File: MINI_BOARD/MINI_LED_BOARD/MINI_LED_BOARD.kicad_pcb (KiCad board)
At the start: 2 copper layers, 75 x 15 mm, 47 parts, among them J1 Conn_ARM_SWD_TagConnect_TC203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, J2 430450428, J3 Conn_01x03_Socket, U1 MSPM0C1103SDDFR, U2 TCAN334, U4 TPS76333DBVR

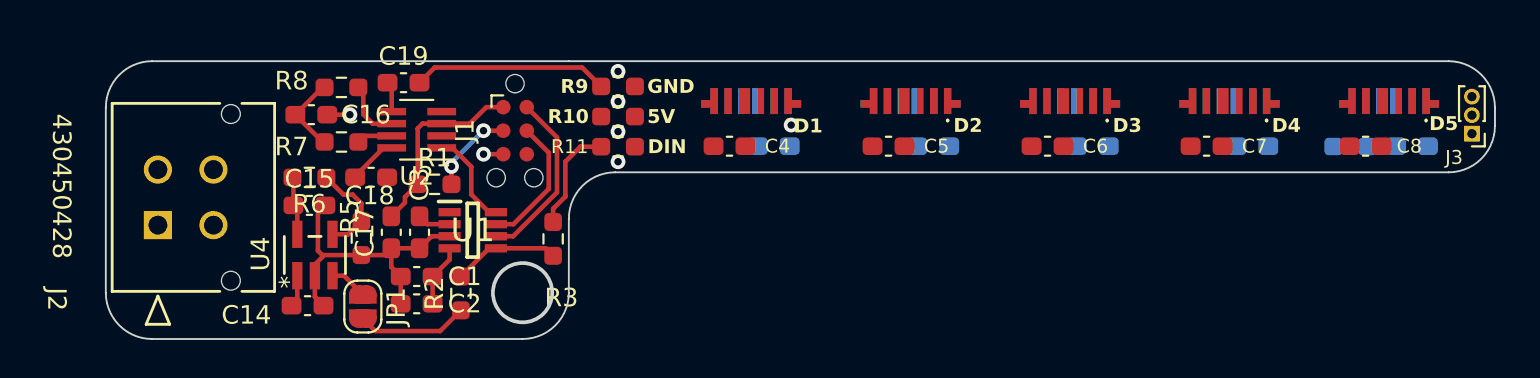
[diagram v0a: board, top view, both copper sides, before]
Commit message: Complete MCU side routing
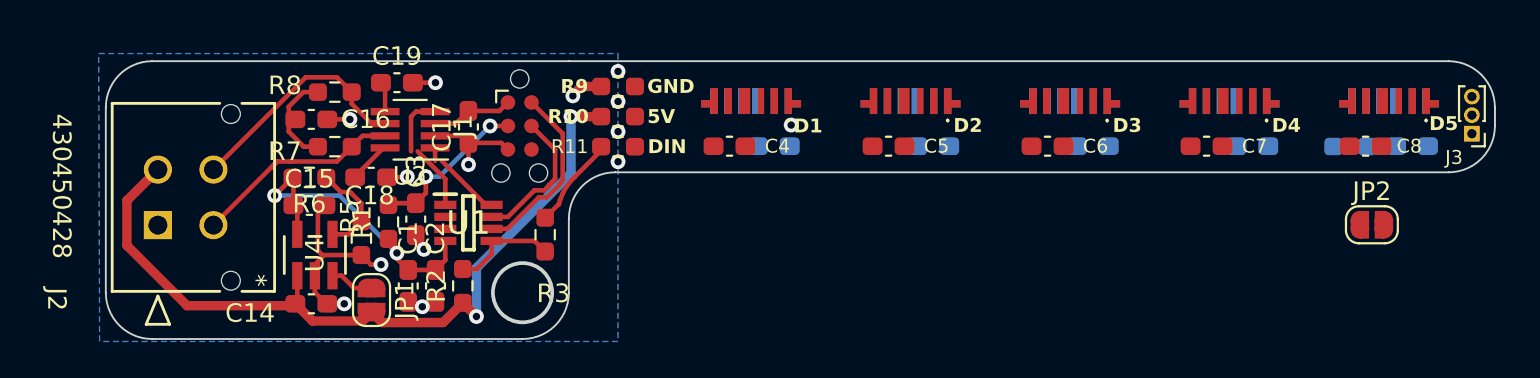
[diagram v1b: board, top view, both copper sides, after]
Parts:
- added JP2: SolderJumper_2_Open, Jumper:SolderJumper-2_P1.3mm_Open_RoundedPad1.0x1.5mm, F.Cu at (116.1, 61.9)
- moved C17 7.05 mm to (67.4, 56.6)
- moved R1 3.21 mm to (63.0, 61.8), turned to 90 degrees
- moved C2 1.40 mm to (65.6, 65.2), turned to -90 degrees
- moved C3 0.74 mm to (64.5, 61.6)
- moved C1 0.68 mm to (64.1, 65.2), turned to -90 degrees
- moved JP1 0.59 mm to (62.1, 66.0)
- moved R3 0.49 mm to (71.5, 62.5)
- moved U1 0.46 mm to (67.4, 61.8)
- moved R7 0.44 mm to (60.1, 57.7)
- moved R8 0.44 mm to (60.1, 54.8)
- moved R2 0.42 mm to (67.1, 65.2)
- moved J1 0.36 mm to (70.1, 56.6)
- moved C19 0.36 mm to (63.5, 54.3)
- moved U2 0.36 mm to (64.2, 56.8)
- moved C16 0.25 mm to (58.9, 56.2)
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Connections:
- J2 pad 3: Net-(U2-CANL) -> Net-(U2-CANH)
- J2 pad 4: Net-(U2-CANH) -> Net-(U2-CANL)
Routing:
- net +5V: track 7.79 -> 42.7 mm, vias 0 -> 2
- net Net-(U2-CANH): track 1.94 -> 11.7 mm
- net Net-(U2-CANL): track 3.36 -> 12.7 mm
- net Net-(U1-PA27_/_A0/UART_TX): track 0.00 -> 6.79 mm
- net GND: track 29.6 -> 23.9 mm, vias 2 -> 9
- net +3.3V: track 17.0 -> 22.2 mm, vias 0 -> 2
- net Net-(J1-~{RESET}): track 6.48 -> 9.10 mm
- net Net-(U1-PA24_/_A3/UART_RX): track 5.24 -> 4.38 mm
- net Net-(R11-Pad2): track 5.80 -> 5.00 mm
- net Net-(C16-Pad1): track 4.37 -> 5.16 mm
- net Net-(J1-SWCLK): track 7.27 -> 7.95 mm
- added copper zone on B.Cu, net GND

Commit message: Route LED side
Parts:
- removed JP2: SolderJumper_2_Open, Jumper:SolderJumper-2_P1.3mm_Open_RoundedPad1.0x1.5mm
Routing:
- net VDD: track 0.00 -> 129.1 mm, vias 0 -> 2
- net Net-(D10-DIN): track 0.00 -> 21.1 mm
- net Net-(D7-DOUT): track 0.00 -> 20.6 mm
- net GND2: track 0.00 -> 18.4 mm, vias 0 -> 1
- net Net-(D2-DOUT): track 0.00 -> 7.50 mm
- net Net-(D1-DOUT): track 0.00 -> 7.48 mm
- net Net-(D3-DOUT): track 0.00 -> 7.47 mm
- net Net-(D4-DOUT): track 0.00 -> 7.45 mm
- net Net-(D1-DIN): track 0.00 -> 4.79 mm
- net Net-(D10-DOUT): track 0.00 -> 4.20 mm
- net (no net): vias 5 -> 4
- added copper zone on B.Cu, net GND2
- added copper zone on F.Cu, net GND2

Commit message: Fix mcu side routing and update mcu-led jumper resistor pads
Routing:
- net +3.3V: track 22.2 -> 33.6 mm, vias 2 -> 3
- net GND: track 23.9 -> 24.9 mm, vias 9 -> 10
- net GND2: track 18.4 -> 19.1 mm

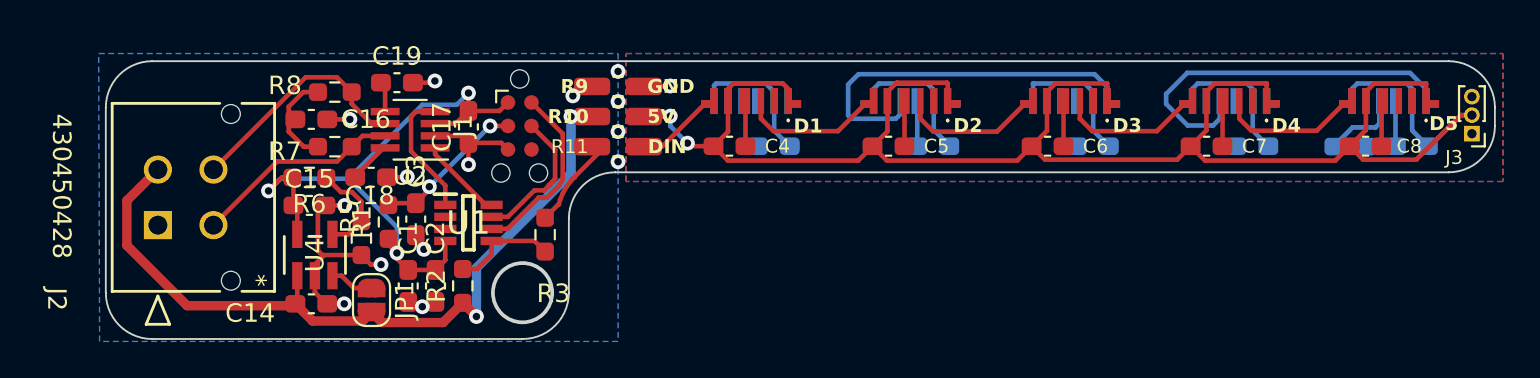
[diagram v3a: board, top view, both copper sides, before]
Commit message: More LED side routing changes
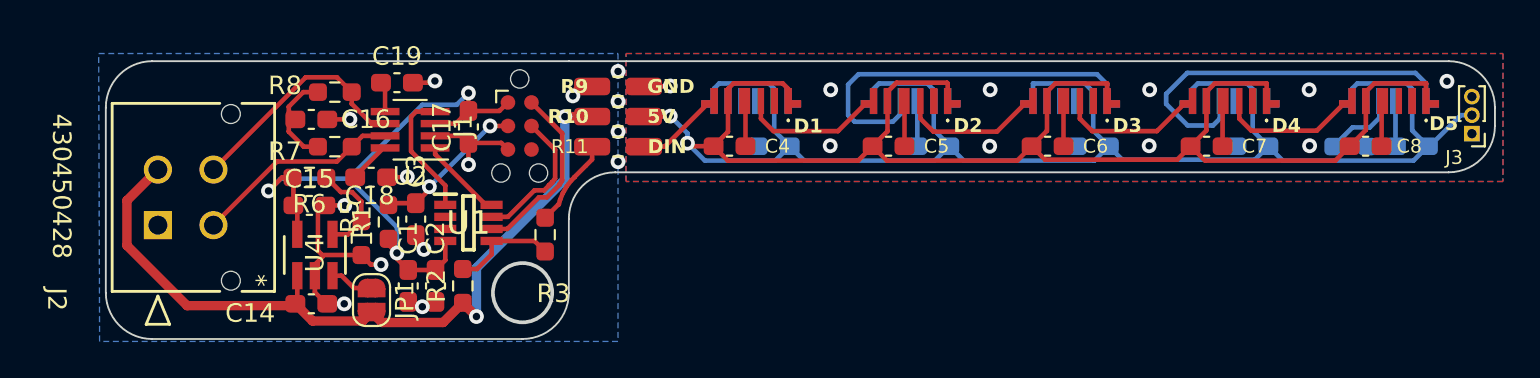
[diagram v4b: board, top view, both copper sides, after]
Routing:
- net VDD: track 129.4 -> 164.7 mm
- net GND2: vias 1 -> 10

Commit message: Clean up silkscreen; route more LED side signals
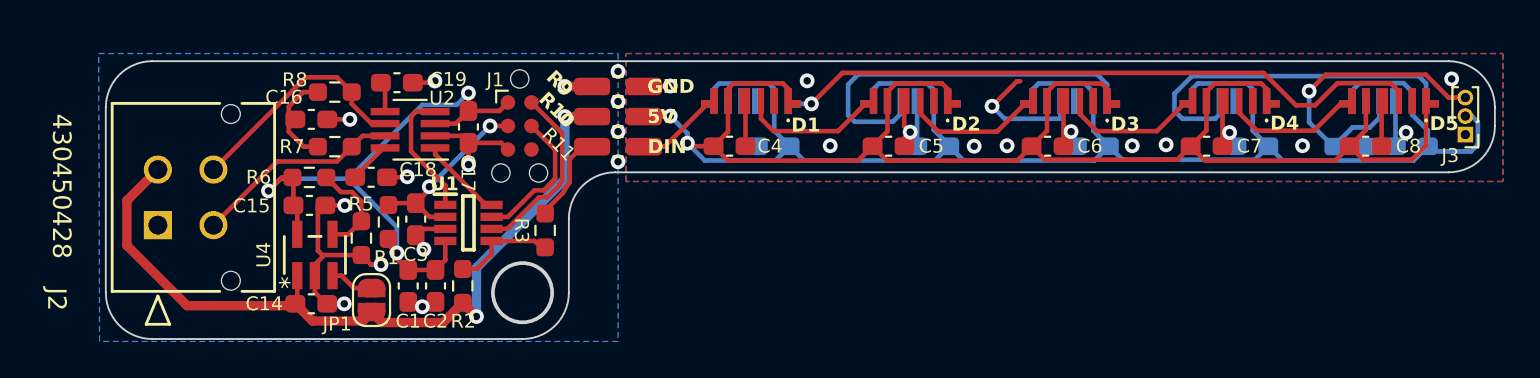
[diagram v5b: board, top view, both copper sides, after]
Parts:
- moved J3 0.36 mm to (121.2, 57.1)
- moved R3 0.23 mm to (71.5, 62.2)
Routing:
- net Net-(D5-DOUT): track 0.00 -> 35.1 mm, vias 0 -> 1
- net Net-(D10-DOUT): track 4.02 -> 16.9 mm, vias 0 -> 1
- net Net-(D8-DOUT): track 0.00 -> 7.00 mm, vias 0 -> 1
- net VDD: track 164.7 -> 168.1 mm
- net GND: track 24.9 -> 26.9 mm
- net Net-(J1-~{RESET}): track 8.67 -> 10.6 mm
- net Net-(D10-DIN): track 21.2 -> 20.0 mm
- net Net-(J1-SWCLK): track 7.95 -> 8.82 mm
- net GND2: track 19.1 -> 19.3 mm, vias 10 -> 13

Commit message: Route last LED signals, still need to fix GND connections
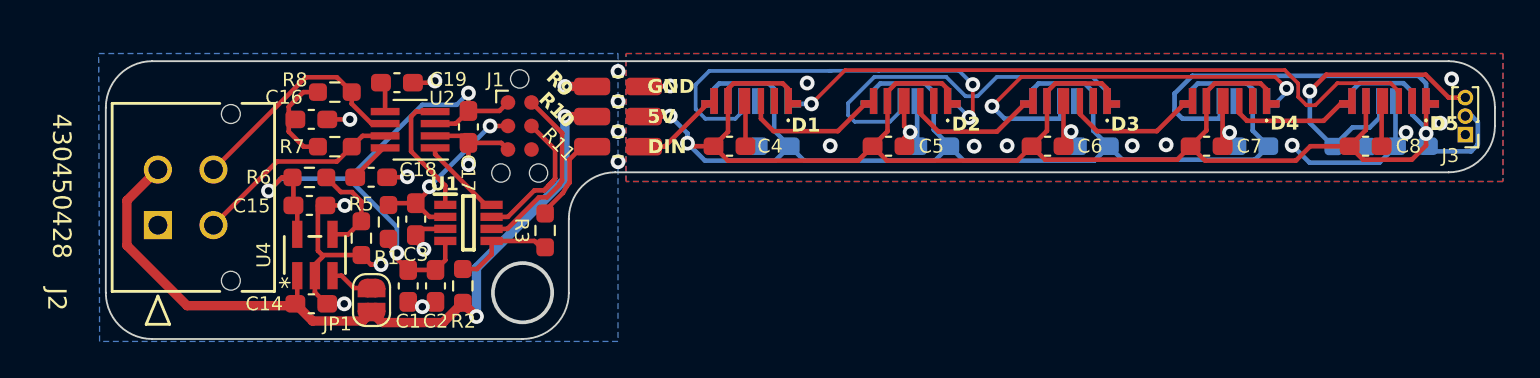
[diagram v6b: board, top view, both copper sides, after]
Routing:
- net Net-(D6-DOUT): track 0.00 -> 23.3 mm, vias 0 -> 2
- net Net-(D8-DOUT): track 7.00 -> 22.8 mm, vias 1 -> 2
- net VDD: track 168.1 -> 158.8 mm, vias 2 -> 3
- net GND2: track 19.3 -> 25.7 mm, vias 13 -> 14
- net Net-(D5-DOUT): track 35.1 -> 35.7 mm

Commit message: Fix LED GND connection
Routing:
- net GND2: track 25.7 -> 41.0 mm
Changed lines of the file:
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@@
   (segment (start 99.318 56.1974) (end 99.316 56.1994) (width 0.25) (layer "B.Cu") (net 25))
   (segment (start 99.318 55.2474) (end 99.318 56.1974) (width 0.25) (layer "B.Cu") (net 25))
-  (segment (start 118.6496 53.8818) (end 106.443 53.8818) (width 0.25) (layer "B.Cu") (net 27))
+  (segment (start 105.4862 54.8386) (end 105.4862 55.7784) (width 0.25) (layer "B.Cu") (net 27))
+  (segment (start 105.4862 55.7784) (end 105.9072 56.1994) (width 0.25) (layer "B.Cu") (net 27))
+  (segment (start 119.0652 54.2974) (end 118.6706 53.9028) (width 0.25) (layer "B.Cu") (net 27))
+  (segment (start 107.9291 56.1974) (end 107.9291 55.2474) (width 0.25) (layer "B.Cu") (net 27))
   (segment (start 119.0652 55.2474) (end 119.0652 54.2974) (width 0.25) (layer "B.Cu") (net 27))
+  (segment (start 118.6706 53.9028) (end 106.422 53.9028) (width 0.25) (layer "B.Cu") (net 27))
   (segment (start 105.9072 56.1994) (end 107.9271 56.1994) (width 0.25) (layer "B.Cu") (net 27))
-  (segment (start 105.4862 54.8386) (end 105.4862 55.7784) (width 0.25) (layer "B.Cu") (net 27))
-  (segment (start 119.0652 54.2974) (end 118.6496 53.8818) (width 0.25) (layer "B.Cu") (net 27))
-  (segment (start 106.443 53.8818) (end 105.4862 54.8386) (width 0.25) (layer "B.Cu") (net 27))
-  (segment (start 107.9291 56.1974) (end 107.9291 55.2474) (width 0.25) (layer "B.Cu") (net 27))
+  (segment (start 106.422 53.9028) (end 105.4862 54.8386) (width 0.25) (layer "B.Cu") (net 27))
   (segment (start 119.2152 55.3974) (end 119.0652 55.2474) (width 0.25) (layer "B.Cu") (net 27))
-  (segment (start 105.4862 55.7784) (end 105.9072 56.1994) (width 0.25) (layer "B.Cu") (net 27))
   (segment (start 107.9271 56.1994) (end 107.9291 56.1974) (width 0.25) (layer "B.Cu") (net 27))
   (segment (start 119.5152 55.3974) (end 119.2152 55.3974) (width 0.25) (layer "B.Cu") (net 27))
@@
   (via (at 99.8982 56.896) (size 0.8) (drill 0.4) (layers "F.Cu" "B.Cu") (net 40))
   (via (at 105.029 57.6072) (size 0.8) (drill 0.4) (layers "F.Cu" "B.Cu") (free) (net 40))
+  (segment (start 119.9702 53.5746) (end 105.3786 53.5746) (width 0.1524) (layer "B.Cu") (net 40))
   (segment (start 91.595725 57.6834) (end 91.5819 57.669575) (width 0.25) (layer "B.Cu") (net 40))
   (segment (start 117.4152 55.2474) (end 117.4152 57.6611) (width 0.25) (layer "B.Cu") (net 40))
+  (segment (start 105.3786 53.5746) (end 105.3084 53.6448) (width 0.1524) (layer "B.Cu") (net 40))
   (segment (start 111.8362 57.6326) (end 112.776 58.5724) (width 0.25) (layer "B.Cu") (net 40))
   (segment (start 117.4152 57.6611) (end 117.4375 57.6834) (width 0.25) (layer "B.Cu") (net 40))
   (segment (start 91.5819 57.669575) (end 91.5819 55.2474) (width 0.25) (layer "B.Cu") (net 40))
+  (segment (start 120.4468 54.0512) (end 119.9702 53.5746) (width 0.1524) (layer "B.Cu") (net 40))
   (segment (start 112.776 58.5724) (end 116.5485 58.5724) (width 0.25) (layer "B.Cu") (net 40))
   (segment (start 116.5485 58.5724) (end 117.4375 57.6834) (width 0.25) (layer "B.Cu") (net 40))

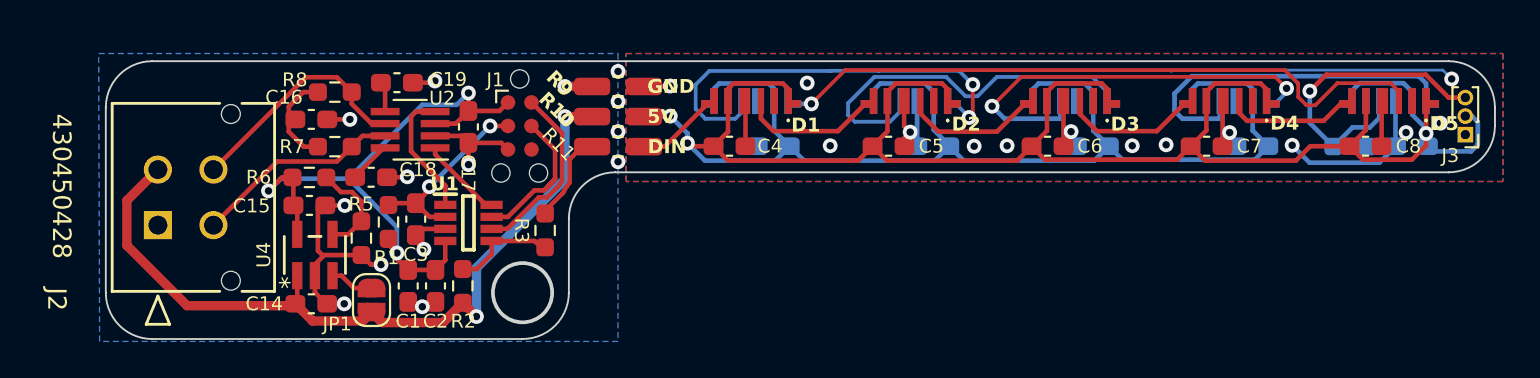
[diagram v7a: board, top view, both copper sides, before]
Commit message: Enlarge LED 5V track, adjust routing accordingly
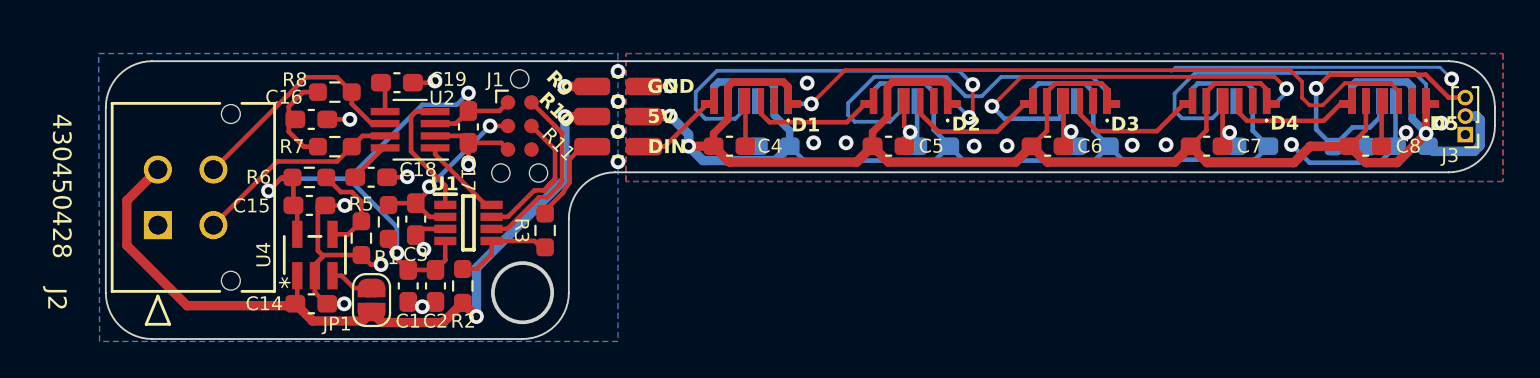
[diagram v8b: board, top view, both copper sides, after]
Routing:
- net VDD: track 158.8 -> 160.2 mm
- net Net-(D1-DOUT): track 7.48 -> 6.92 mm
- net GND2: track 41.0 -> 41.2 mm, vias 14 -> 15
